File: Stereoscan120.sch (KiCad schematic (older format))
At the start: 2 parts

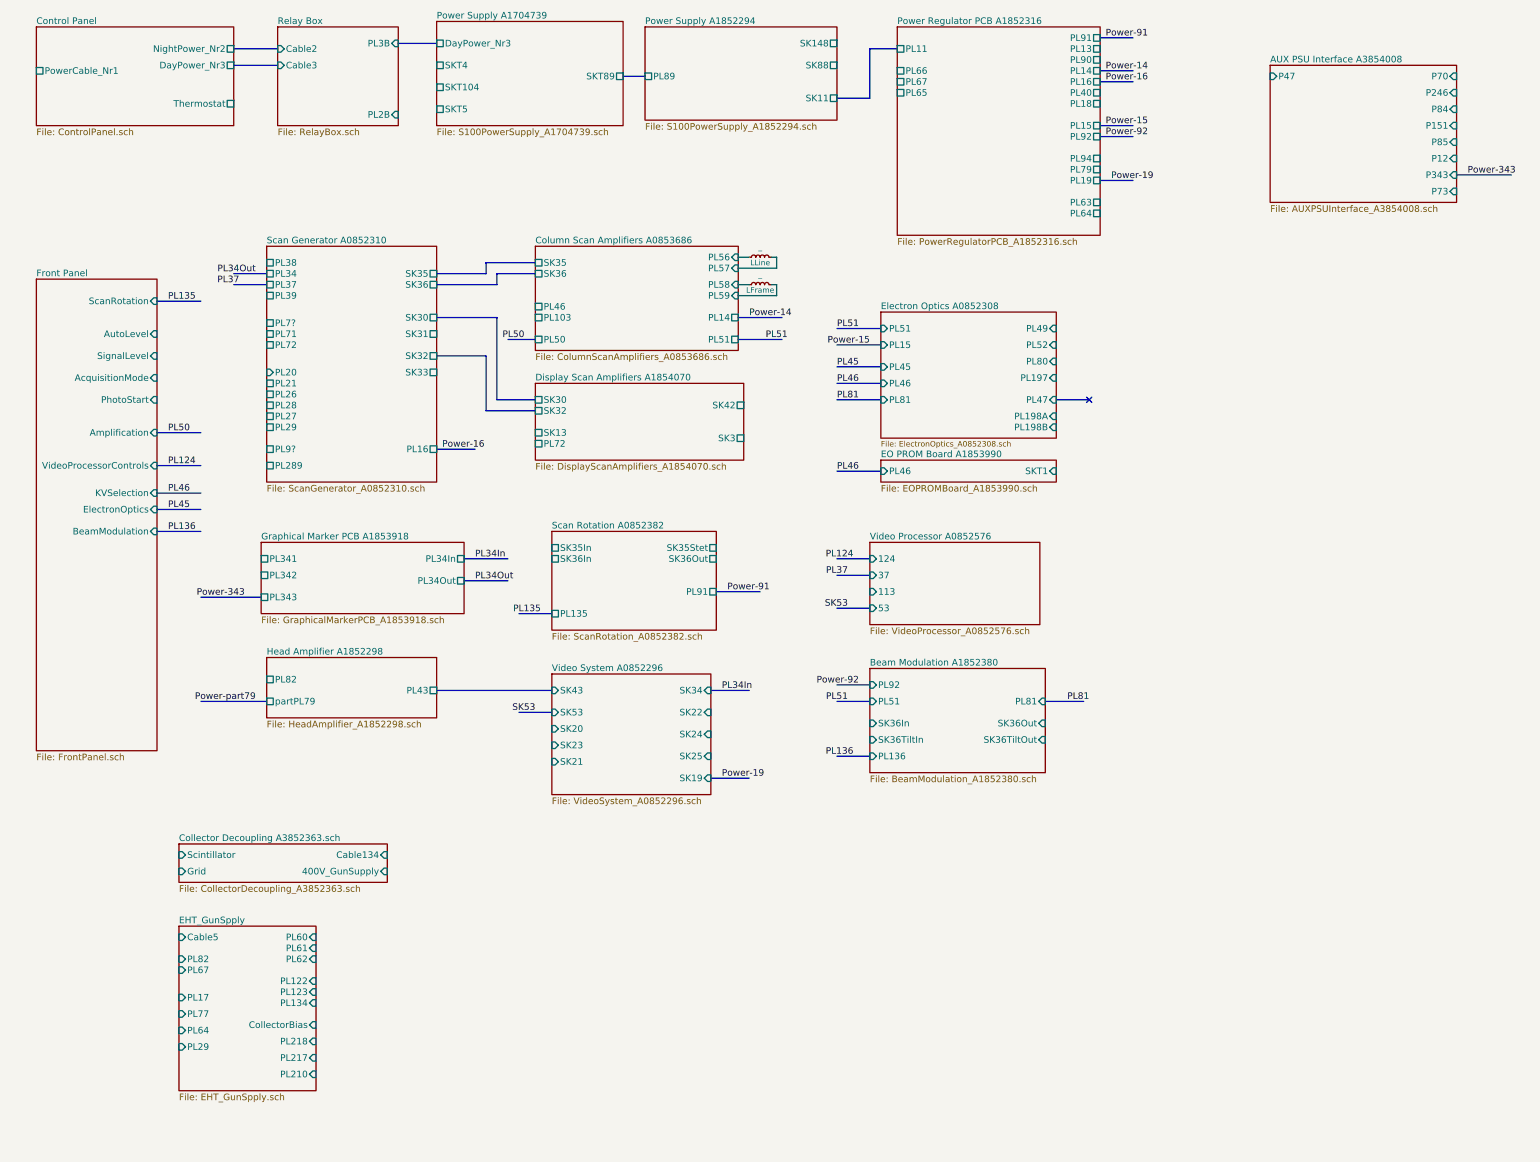
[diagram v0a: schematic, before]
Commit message: added ColumnWiring, DataSystemAutoReset, KVSelection and VacuumInterlock
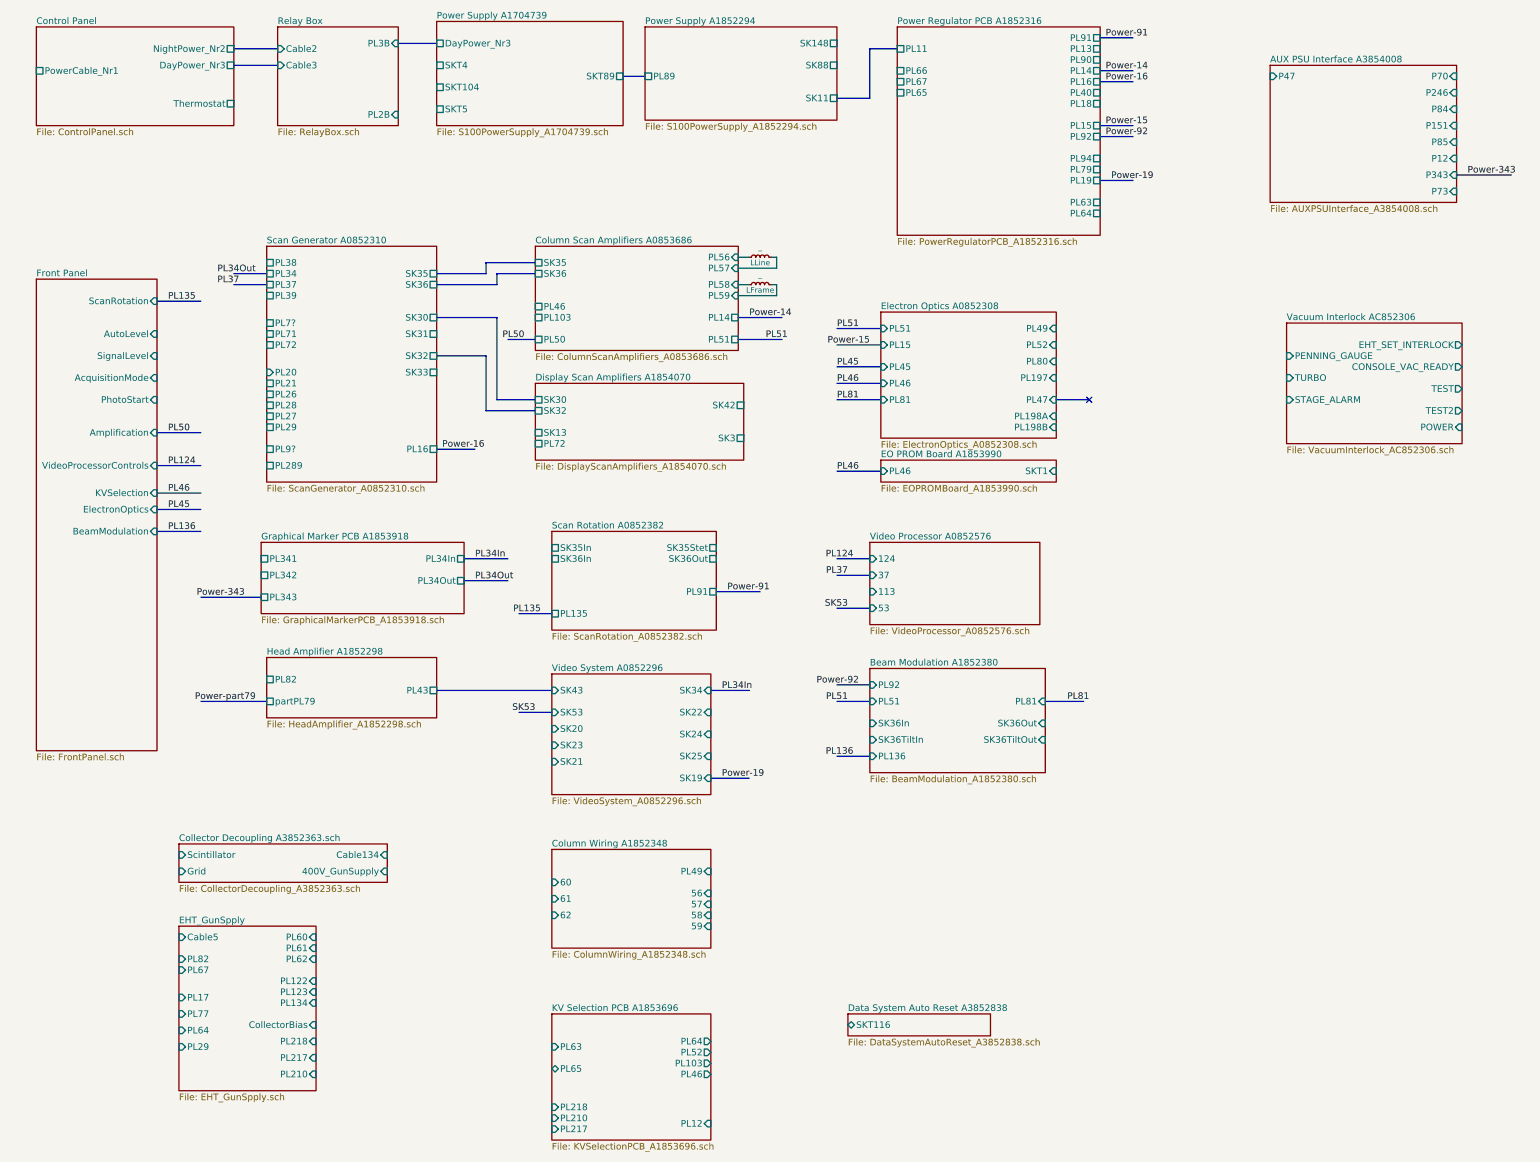
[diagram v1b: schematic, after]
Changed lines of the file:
@@
 LIBS:transistors
 LIBS:conn
+LIBS:linear
 LIBS:regul
 LIBS:74xx
@@
 LIBS:relays
 LIBS:Stereoscan120-cache
-EELAYER 26 0
+EELAYER 25 0
 EELAYER END
 $Descr A3 16535 11693
 encoding utf-8
-Sheet 1 21
+Sheet 1 25
 Title ""
 Date ""
@@
 U 5B0CE4F6
 F0 "Electron Optics A0852308" 60
-F1 "ElectronOptics_A0852308.sch" 0
+F1 "ElectronOptics_A0852308.sch" 60
 F2 "PL51" I L 8400 3550 60
 F3 "PL45" I L 8400 3900 60
@@
 F18 "PL210" I R 3250 10350 60
 $EndSheet
+$Sheet
+S 5400 8300 1450 900
+U 5B1A316B
+F0 "Column Wiring A1852348" 60
+F1 "ColumnWiring_A1852348.sch" 60
+F2 "PL49" I R 6850 8500 60
+F3 "56" I R 6850 8700 60
+F4 "60" I L 5400 8600 60
+F5 "61" I L 5400 8750 60
+F6 "62" I L 5400 8900 60
+F7 "57" I R 6850 8800 60
+F8 "58" I R 6850 8900 60
+F9 "59" I R 6850 9000 60
+$EndSheet
+$Sheet
+S 5400 9800 1450 1150
+U 5B1FEBEE
+F0 "KV Selection PCB A1853696" 60
+F1 "KVSelectionPCB_A1853696.sch" 60
+F2 "PL64" O R 6850 10050 60
+F3 "PL52" O R 6850 10150 60
+F4 "PL103" O R 6850 10250 60
+F5 "PL46" O R 6850 10350 60
+F6 "PL12" I R 6850 10800 60
+F7 "PL217" I L 5400 10850 60
+F8 "PL210" I L 5400 10750 60
+F9 "PL218" I L 5400 10650 60
+F10 "PL65" B L 5400 10300 60
+F11 "PL63" I L 5400 10100 60
+$EndSheet
+$Sheet
+S 8100 9800 1300 200
+U 5B20E7C1
+F0 "Data System Auto Reset A3852838" 60
+F1 "DataSystemAutoReset_A3852838.sch" 60
+F2 "SKT116" B L 8100 9900 60
+$EndSheet
+$Sheet
+S 12100 3500 1600 1100
+U 5B21CAA7
+F0 "Vacuum Interlock AC852306" 60
+F1 "VacuumInterlock_AC852306.sch" 60
+F2 "EHT_SET_INTERLOCK" O R 13700 3700 60
+F3 "CONSOLE_VAC_READY" O R 13700 3900 60
+F4 "TEST" O R 13700 4100 60
+F5 "TEST2" O R 13700 4300 60
+F6 "POWER" I R 13700 4450 60
+F7 "PENNING_GAUGE" I L 12100 3800 60
+F8 "TURBO" I L 12100 4000 60
+F9 "STAGE_ALARM" I L 12100 4200 60
+$EndSheet
 $EndSCHEMATC
